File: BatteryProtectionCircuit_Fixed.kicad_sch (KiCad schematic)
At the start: 40 parts, among them J2 Conn_01x07_Pin, Q1 NMOS, U2 LM358, U3 LM358, U4 LM321, U6 LMC555xN

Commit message: Fixed based on Design Review Feedback
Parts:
- added C1: 1uF, symbol Device:C
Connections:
- net GND: now also C1.2
- net REL: now also K2.1; no longer K2.2
- net VIN: now also U6.4 (R)
- net at U6.5 (CV): now also C1.1
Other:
- moved on the sheet: C2, R26, U6
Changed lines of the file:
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@@
 	)
 	(rectangle
-		(start 85.09 82.55)
+		(start 76.2 82.55)
 		(end 127 114.3)
 		(stroke
@@
 	(text "Monotable 555 Timer"
 		(exclude_from_sim no)
-		(at 106.934 81.28 0)
+		(at 98.044 81.28 0)
 		(effects
 			(font
@@
 	)
 	(junction
+		(at 111.76 74.93)
+		(diameter 0)
+		(color 0 0 0 0)
+	)
+	(junction
 		(at 203.2 104.14)
 		(diameter 0)
@@
 	)
 	(junction
-		(at 97.79 101.6)
+		(at 88.9 101.6)
 		(diameter 0)
 		(color 0 0 0 0)
@@
 	)
 	(junction
-		(at 97.79 96.52)
+		(at 88.9 96.52)
 		(diameter 0)
 		(color 0 0 0 0)
@@
 	)
 	(junction
-		(at 116.84 71.12)
-		(diameter 0)
-		(color 0 0 0 0)
-	)
-	(junction
 		(at 157.48 129.54)
 		(diameter 0)
@@
 	(wire
 		(pts
+			(xy 111.76 74.93) (xy 111.76 71.12)
+		)
+		(stroke
+			(width 0)
+			(type default)
+		)
+	)
+	(wire
+		(pts
 			(xy 191.77 80.01) (xy 187.96 80.01)
 		)
@@
 	(wire
 		(pts
-			(xy 97.79 104.14) (xy 97.79 101.6)
+			(xy 88.9 104.14) (xy 88.9 101.6)
 		)
 		(stroke
@@
 	(wire
 		(pts
+			(xy 111.76 74.93) (xy 111.76 77.47)
+		)
+		(stroke
+			(width 0)
+			(type default)
+		)
+	)
+	(wire
+		(pts
 			(xy 185.42 116.84) (xy 187.96 116.84)
 		)
@@
 	(wire
 		(pts
-			(xy 97.79 101.6) (xy 97.79 96.52)
+			(xy 88.9 101.6) (xy 88.9 96.52)
 		)
 		(stroke
@@
 	(wire
 		(pts
+			(xy 125.73 74.93) (xy 111.76 74.93)
+		)
+		(stroke
+			(width 0)
+			(type default)
+		)
+	)
+	(wire
+		(pts
 			(xy 152.4 68.58) (xy 165.1 68.58)
 		)
@@
 	(wire
 		(pts
-			(xy 116.84 71.12) (xy 116.84 76.2)
-		)
-		(stroke
-			(width 0)
-			(type default)
-		)
-	)
-	(wire
-		(pts
 			(xy 135.89 91.44) (xy 146.05 91.44)
 		)
@@
 	(wire
 		(pts
-			(xy 110.49 106.68) (xy 110.49 113.03)
+			(xy 101.6 106.68) (xy 101.6 113.03)
 		)
 		(stroke
@@
 	(wire
 		(pts
-			(xy 116.84 71.12) (xy 125.73 71.12)
-		)
-		(stroke
-			(width 0)
-			(type default)
-		)
-	)
-	(wire
-		(pts
-			(xy 125.73 71.12) (xy 125.73 67.31)
+			(xy 125.73 67.31) (xy 125.73 74.93)
 		)
 		(stroke
@@
 	(wire
 		(pts
-			(xy 97.79 111.76) (xy 97.79 113.03)
+			(xy 88.9 111.76) (xy 88.9 113.03)
 		)
 		(stroke
@@
 	(wire
 		(pts
-			(xy 90.17 91.44) (xy 97.79 91.44)
+			(xy 81.28 91.44) (xy 88.9 91.44)
 		)
 		(stroke
@@
 	)
 	(label "TR"
-		(at 123.19 91.44 0)
+		(at 114.3 91.44 0)
 		(effects
 			(font
@@
 	)
 	(label "OUT"
-		(at 90.17 91.44 180)
+		(at 81.28 91.44 180)
 		(effects
 			(font
@@
 		)
 	)
+	(label "VIN"
+		(at 114.3 101.6 0)
+		(effects
+			(font
+				(size 1.27 1.27)
+			)
+			(justify left bottom)
+		)
+	)
 	(label "D51"
 		(at 217.17 128.27 0)
@@
 	)
 	(label "VIN"
-		(at 90.17 96.52 180)
+		(at 81.28 96.52 180)
 		(effects
 			(font
@@
 	)
 	(label "VIN"
-		(at 110.49 86.36 0)
+		(at 101.6 86.36 0)
 		(effects
 			(font
@@
 	)
 	(label "GND"
-		(at 97.79 113.03 0)
+		(at 88.9 113.03 0)
 		(effects
 			(font
@@
 	)
 	(label "GND"
-		(at 110.49 113.03 0)
+		(at 101.6 113.03 0)
 		(effects
 			(font
@@
 		)
 	)
+	(label "GND"
+		(at 121.92 96.52 0)
+		(effects
+			(font
+				(size 1.27 1.27)
+			)
+			(justify left bottom)
+		)
+	)
 	(label "VD"
 		(at 166.37 129.54 0)
@@
 	)
 	(label "REL"
-		(at 116.84 76.2 0)
+		(at 111.76 77.47 180)
 		(effects
 			(font
 				(size 1.27 1.27)
 			)
-			(justify left bottom)
+			(justify right bottom)
 		)
 	)
@@
 	)
 	(symbol
+		(lib_id "Device:C")
+		(at 118.11 96.52 90)
+		(unit 1)
+		(exclude_from_sim no)
+		(in_bom yes)
+		(on_board yes)
+		(dnp no)
+		(property "Reference" "C1"
+			(at 120.142 91.186 90)
+			(effects
+				(font
+					(size 1.27 1.27)
+				)
+			)
+		)
+		(property "Value" "1uF"
+			(at 120.142 93.218 90)
+			(effects
+				(font
+					(size 1.27 1.27)
+				)
+			)
+		)
+		(property "Footprint" ""
+			(at 121.92 95.5548 0)
+			(effects
+				(font
+					(size 1.27 1.27)
+				)
+				(hide yes)
+			)
+		)
+		(property "Datasheet" "~"
+			(at 118.11 96.52 0)
+			(effects
+				(font
+					(size 1.27 1.27)
+				)
+				(hide yes)
+			)
+		)
+		(property "Description" "Unpolarized capacitor"
+			(at 118.11 96.52 0)
+			(effects
+				(font
+					(size 1.27 1.27)
+				)
+				(hide yes)
+			)
+		)
+		(pin "2"
+		)
+		(pin "1"
+		)
+		(instances
+			(project ""
+				(path "/299dddd9-ac06-42a6-950e-710b9bcf8f9e"
+					(reference "C1")
+					(unit 1)
+				)
+			)
+		)
+	)
+	(symbol
 		(lib_id "Device:R_US")
 		(at 165.1 124.46 0)
@@
 	(symbol
 		(lib_id "Device:C")
-		(at 97.79 107.95 0)
+		(at 88.9 107.95 0)
 		(mirror x)
 		(unit 1)
@@
 		(dnp no)
 		(property "Reference" "C2"
-			(at 95.25 107.188 0)
+			(at 86.36 107.188 0)
 			(effects
 				(font
@@
 		)
 		(property "Value" "1uF"
-			(at 95.25 108.966 0)
+			(at 86.36 108.966 0)
 			(effects
 				(font
@@
 		)
 		(property "Footprint" "Capacitor_SMD:C_0805_2012Metric"
-			(at 98.7552 104.14 0)
+			(at 89.8652 104.14 0)
 			(effects
 				(font
@@
 		)
 		(property "Datasheet" "~"
-			(at 97.79 107.95 0)
+			(at 88.9 107.95 0)
 			(effects
 				(font
@@
 		)
 		(property "Description" "Unpolarized capacitor"
-			(at 97.79 107.95 0)
+			(at 88.9 107.95 0)
 			(effects
 				(font
@@
 	(symbol
 		(lib_id "Timer:LMC555xN")
-		(at 110.49 96.52 0)
+		(at 101.6 96.52 0)
 		(mirror y)
 		(unit 1)
@@
 		(dnp no)
 		(property "Reference" "U6"
-			(at 98.298 87.122 0)
+			(at 89.408 87.122 0)
 			(effects
 				(font
@@
 		)
 		(property "Value" "LMC555xN"
-			(at 98.298 84.582 0)
+			(at 89.408 84.582 0)
 			(effects
 				(font
@@
 		)
 		(property "Footprint" "Package_DIP:DIP-8_W7.62mm"
-			(at 93.98 106.68 0)
+			(at 85.09 106.68 0)
 			(effects
 				(font
@@
 		)
 		(property "Datasheet" "http://www.ti.com/lit/ds/symlink/lmc555.pdf"
-			(at 88.9 106.68 0)
+			(at 80.01 106.68 0)
 			(effects
 				(font
@@
 		)
 		(property "Description" "CMOS Timer, 555 compatible, PDIP-8"
-			(at 110.49 96.52 0)
+			(at 101.6 96.52 0)
 			(effects
 				(font
@@
 	(symbol
 		(lib_id "Device:R_US")
-		(at 93.98 96.52 90)
+		(at 85.09 96.52 90)
 		(mirror x)
 		(unit 1)
@@
 		(dnp no)
 		(property "Reference" "R26"
-			(at 93.98 100.838 90)
+			(at 85.09 100.838 90)
 			(effects
 				(font
@@
 		)
 		(property "Value" "4.7k"
-			(at 93.98 98.806 90)
+			(at 85.09 98.806 90)
 			(effects
 				(font
@@
 		)
 		(property "Footprint" "Resistor_SMD:R_0805_2012Metric"
-			(at 94.234 97.536 90)
+			(at 85.344 97.536 90)
 			(effects
 				(font
@@
 		)
 		(property "Datasheet" "~"
-			(at 93.98 96.52 0)
+			(at 85.09 96.52 0)
 			(effects
 				(font
@@
 		)
 		(property "Description" "Resistor, US symbol"
-			(at 93.98 96.52 0)
+			(at 85.09 96.52 0)
 			(effects
 				(font

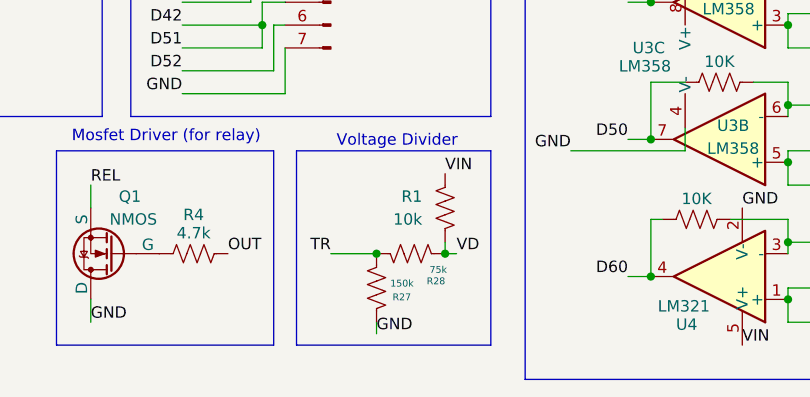
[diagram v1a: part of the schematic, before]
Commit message: Updated voltage divider values
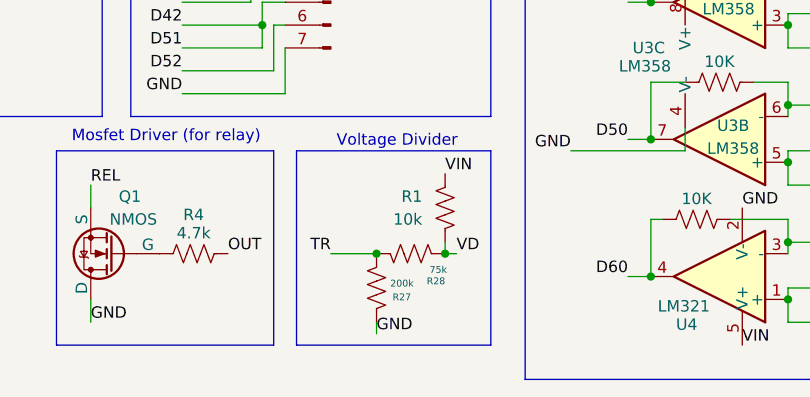
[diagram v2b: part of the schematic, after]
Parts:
- R27: value 150k -> 200k
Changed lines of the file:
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@@
 			)
 		)
-		(property "Value" "150k"
+		(property "Value" "200k"
 			(at 159.004 132.842 0)
 			(effects

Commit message: ERC check fixes
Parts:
- removed unit 3 of U2
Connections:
- net GND: now also U2.4 (V-)
- net VIN renamed +5V
- net +5V: now also U2.8 (V+)
- no-connect marks 0 -> 1
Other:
- moved on the sheet: C2, Q1, R1, R27, R28, R4

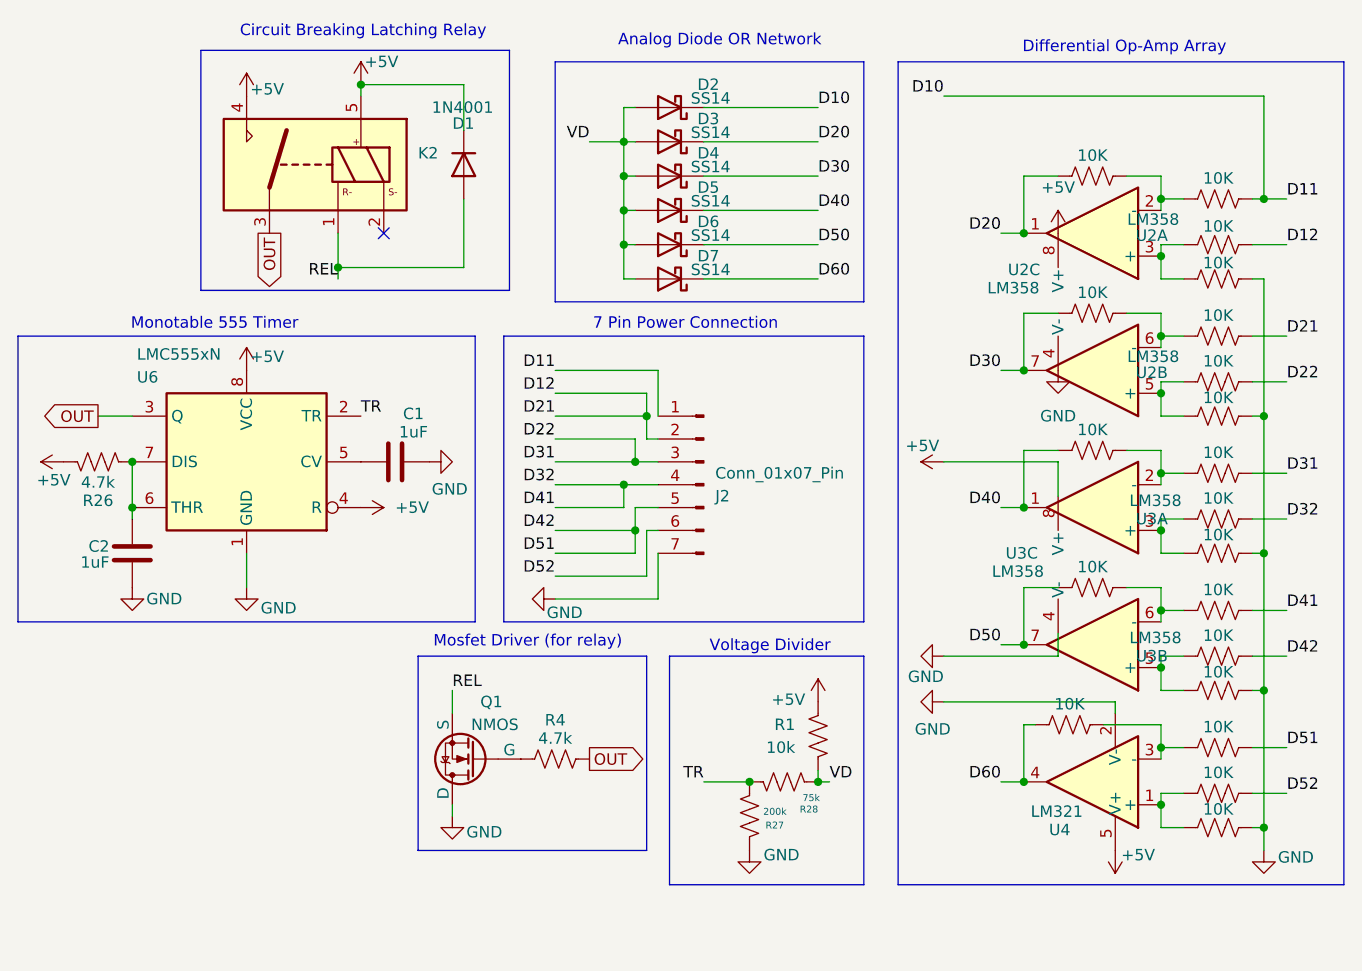
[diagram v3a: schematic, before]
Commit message: LTSPICE simulation + Voltage Divider Fixes
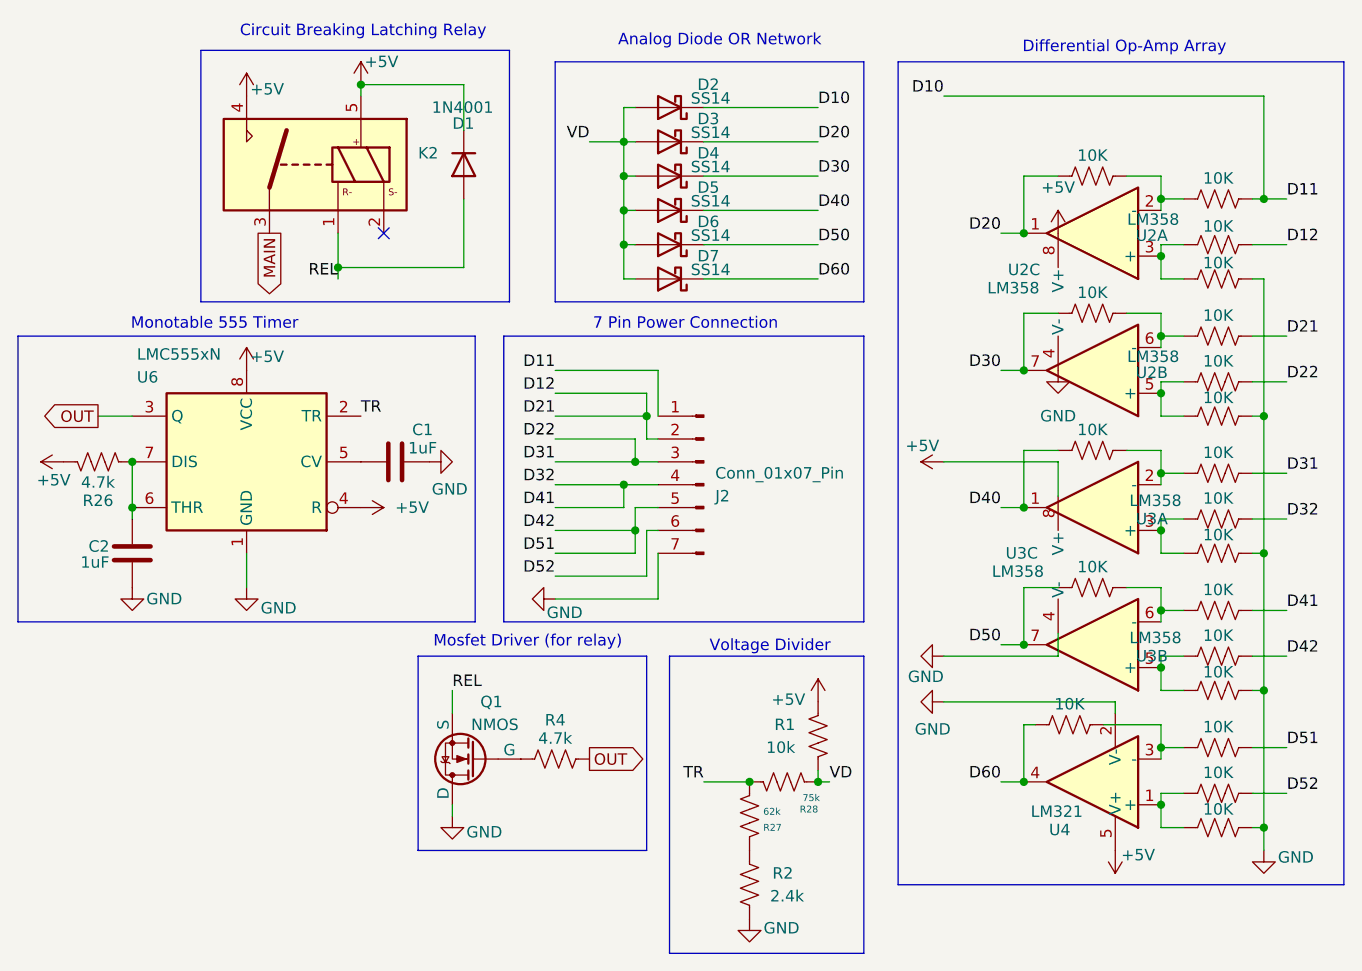
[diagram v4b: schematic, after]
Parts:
- added R2: 2.4k, symbol Device:R_US
- added unit 2 of U2
- R27: value 200k -> 62k
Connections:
- net D30: now also U2.7; no longer U2.7
- net GND: now also R2.2; no longer R27.1
- net OUT: no longer K2.3
- net at R11.1, R12.1: now also U2.5 (+); no longer U2.5 (+)
- net at R10.2, R9.1: now also U2.6 (-); no longer U2.6 (-)
- new net: R2.1, R27.1
- new net MAIN: K2.3
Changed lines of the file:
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@@
 	(rectangle
 		(start 148.59 118.11)
-		(end 170.18 143.51)
+		(end 170.18 151.13)
 		(stroke
 			(width 0)
@@
 	(rectangle
 		(start 96.52 50.8)
-		(end 130.81 77.47)
+		(end 130.81 78.74)
 		(stroke
 			(width 0)
@@
 		)
 	)
-	(global_label "OUT"
+	(global_label "MAIN"
 		(shape output)
 		(at 104.14 71.12 270)
@@
 		)
 		(property "Intersheetrefs" "${INTERSHEET_REFS}"
-			(at 104.14 77.7338 90)
+			(at 104.14 78.5805 90)
 			(effects
 				(font
@@
 		(dnp no)
 		(property "Reference" "R27"
-			(at 159.258 136.9061 0)
+			(at 159.004 137.16 0)
 			(effects
 				(font
@@
 			)
 		)
-		(property "Value" "200k"
+		(property "Value" "62k"
 			(at 159.004 135.382 0)
 			(effects
@@
 		(dnp no)
 		(property "Reference" "C1"
-			(at 120.142 91.186 90)
+			(at 121.158 92.964 90)
 			(effects
 				(font
@@
 		)
 		(property "Value" "1uF"
-			(at 120.142 93.218 90)
+			(at 121.158 94.996 90)
 			(effects
 				(font
@@
 	(symbol
 		(lib_id "power:GND")
+		(at 157.48 147.32 0)
+		(unit 1)
+		(exclude_from_sim no)
+		(in_bom yes)
+		(on_board yes)
+		(dnp no)
+		(property "Reference" "#PWR02"
+			(at 157.48 153.67 0)
+			(effects
+				(font
+					(size 1.27 1.27)
+				)
+				(hide yes)
+			)
+		)
+		(property "Value" "GND"
+			(at 161.036 148.336 0)
+			(effects
+				(font
+					(size 1.27 1.27)
+				)
+			)
+		)
+		(property "Footprint" ""
+			(at 157.48 147.32 0)
+			(effects
+				(font
+					(size 1.27 1.27)
+				)
+				(hide yes)
+			)
+		)
+		(property "Datasheet" ""
+			(at 157.48 147.32 0)
+			(effects
+				(font
+					(size 1.27 1.27)
+				)
+				(hide yes)
+			)
+		)
+		(property "Description" "Power symbol creates a global label with name \"GND\" , ground"
+			(at 157.48 147.32 0)
+			(effects
+				(font
+					(size 1.27 1.27)
+				)
+				(hide yes)
+			)
+		)
+		(pin "1"
+		)
+		(instances
+			(project ""
+				(path "/299dddd9-ac06-42a6-950e-710b9bcf8f9e"
+					(reference "#PWR02")
+					(unit 1)
+				)
+			)
+		)
+	)
+	(symbol
+		(lib_id "power:GND")
 		(at 191.77 86.36 0)
 		(unit 1)
@@
 	)
 	(symbol
+		(lib_id "Device:R_US")
+		(at 157.48 143.51 0)
+		(unit 1)
+		(exclude_from_sim no)
+		(in_bom yes)
+		(on_board yes)
+		(dnp no)
+		(property "Reference" "R2"
+			(at 160.02 142.24 0)
+			(effects
+				(font
+					(size 1.27 1.27)
+				)
+				(justify left)
+			)
+		)
+		(property "Value" "2.4k"
+			(at 159.766 144.78 0)
+			(effects
+				(font
+					(size 1.27 1.27)
+				)
+				(justify left)
+			)
+		)
+		(property "Footprint" ""
+			(at 158.496 143.764 90)
+			(effects
+				(font
+					(size 1.27 1.27)
+				)
+				(hide yes)
+			)
+		)
+		(property "Datasheet" "~"
+			(at 157.48 143.51 0)
+			(effects
+				(font
+					(size 1.27 1.27)
+				)
+				(hide yes)
+			)
+		)
+		(property "Description" "Resistor, US symbol"
+			(at 157.48 143.51 0)
+			(effects
+				(font
+					(size 1.27 1.27)
+				)
+				(hide yes)
+			)
+		)
+		(pin "1"
+		)
+		(pin "2"
+		)
+		(instances
+			(project ""
+				(path "/299dddd9-ac06-42a6-950e-710b9bcf8f9e"
+					(reference "R2")
+					(unit 1)
+				)
+			)
+		)
+	)
+	(symbol
 		(lib_id "Timer:LMC555xN")
 		(at 101.6 96.52 0)
@@
 					(unit 1)
 				)
-			)
-		)
-	)
-	(symbol
-		(lib_id "power:GND")
-		(at 157.48 139.7 0)
-		(unit 1)
-		(exclude_from_sim no)
-		(in_bom yes)
-		(on_board yes)
-		(dnp no)
-		(property "Reference" "#PWR014"
-			(at 157.48 146.05 0)
-			(effects
-				(font
-					(size 1.27 1.27)
-				)
-				(hide yes)
-			)
-		)
-		(property "Value" "GND"
-			(at 161.036 140.208 0)
-			(effects
-				(font
-					(size 1.27 1.27)
-				)
-			)
-		)
-		(property "Footprint" ""
-			(at 157.48 139.7 0)
-			(effects
-				(font
-					(size 1.27 1.27)
-				)
-				(hide yes)
-			)
-		)
-		(property "Datasheet" ""
-			(at 157.48 139.7 0)
-			(effects
-				(font
-					(size 1.27 1.27)
-				)
-				(hide yes)
-			)
-		)
-		(property "Description" "Power symbol creates a global label with name \"GND\" , ground"
-			(at 157.48 139.7 0)
-			(effects
-				(font
-					(size 1.27 1.27)
-				)
-				(hide yes)
-			)
-		)
-		(pin "1"
-		)
-		(instances
-			(project ""
-				(path "/299dddd9-ac06-42a6-950e-710b9bcf8f9e"
-					(reference "#PWR014")
-					(unit 1)
-				)
